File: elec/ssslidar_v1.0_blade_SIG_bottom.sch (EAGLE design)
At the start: 25 parts, among them P10 PIN_SMD_1X1_RECT, P11 PIN_SMD_1X2, P12 PIN_SMD_1X1_RECT, P13 PIN_SMD_1X1_RECT, P15 PIN_SMD_0.8X1_RECT, P16 PIN_SMD_1X1_RECT, P17 PIN_SMD_1X2, P18 PIN_SMD_0.8X1_RECT, P19 PIN_SMD_0.8X1_RECT, P2 PIN_SMD_1X1_RECT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

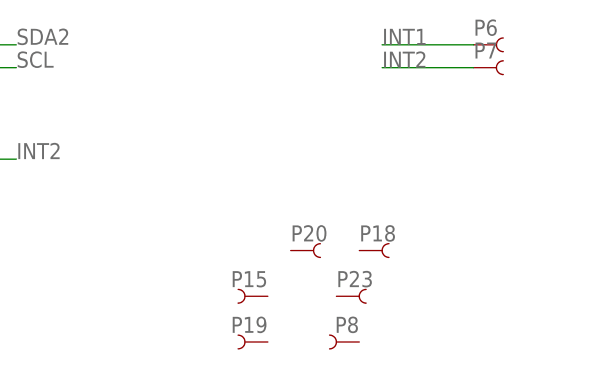
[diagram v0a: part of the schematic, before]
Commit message: Separated blades into bottom and top, since the bottom ones need to be taller to avoid seeing the Main PCB, or the screws...
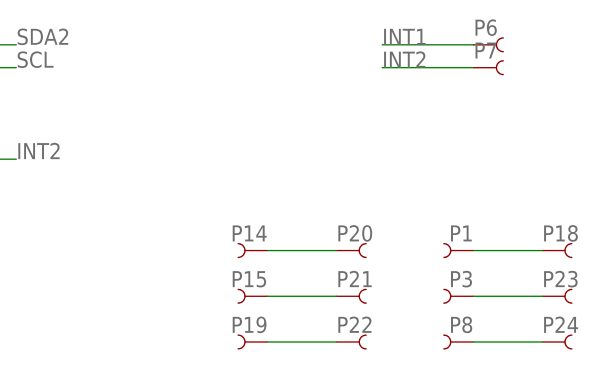
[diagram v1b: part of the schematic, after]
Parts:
- added P1, P14, P21, P22, P24, P3: PIN_SMD_0.8X1_RECT, Xevelabs:PIN_SMD_0.8X1_RECT
- P10, P12, P13, P16, P2, P9: value PIN_SMD_1X1_RECT -> PIN_SMD_1X2; device Xevelabs:PIN_SMD_1X1_RECT -> Xevelabs:PIN_SMD_1X2
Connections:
- new net N$1: P14.1, P20.1
- new net N$2: P15.1, P21.1
- new net N$3: P19.1, P22.1
- new net N$4: P1.1, P18.1
- new net N$5: P23.1, P3.1
- new net N$6: P24.1, P8.1
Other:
- moved on the sheet: P18, P20, P23, P8
